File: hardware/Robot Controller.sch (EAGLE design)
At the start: 7 parts

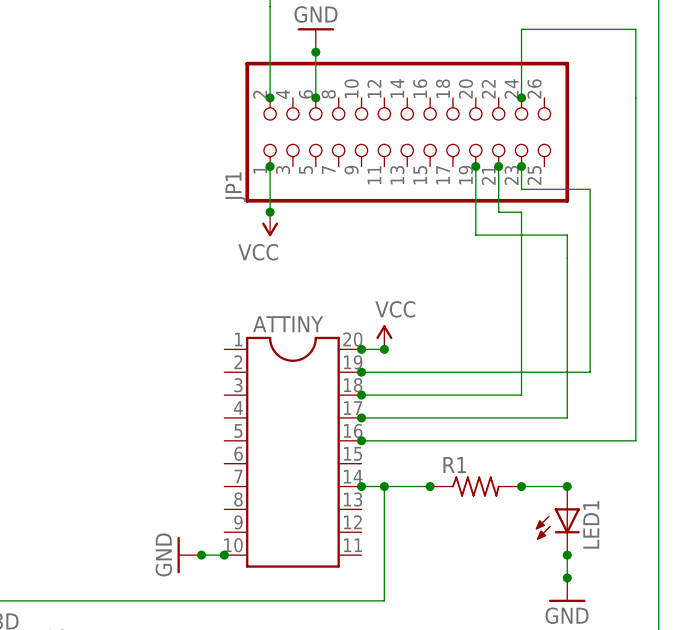
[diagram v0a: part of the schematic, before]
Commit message: added a host pin
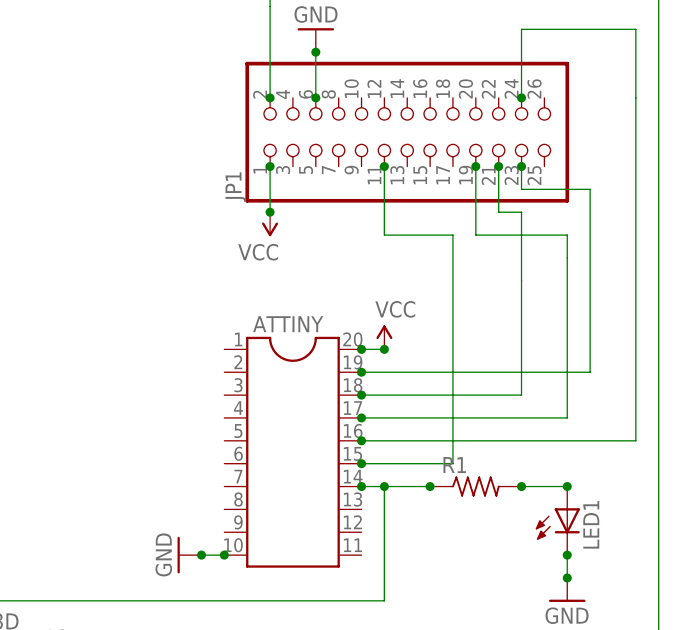
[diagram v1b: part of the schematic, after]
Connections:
- new net N$2: ATTINY.15, JP1.11
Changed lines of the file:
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@@
+</segment>
+</net>
+<net name="N$2" class="0">
+<segment>
+<pinref part="JP1" gate="A" pin="11"/>
+<wire x1="68.58" y1="93.98" x2="68.58" y2="86.36" width="0.1524" layer="91"/>
+<wire x1="68.58" y1="86.36" x2="76.2" y2="86.36" width="0.1524" layer="91"/>
+<wire x1="76.2" y1="86.36" x2="76.2" y2="60.96" width="0.1524" layer="91"/>
+<pinref part="ATTINY" gate="G$1" pin="15"/>
+<wire x1="76.2" y1="60.96" x2="66.04" y2="60.96" width="0.1524" layer="91"/>
+<junction x="66.04" y="60.96"/>
+<junction x="68.58" y="93.98"/>
 </segment>
 </net>

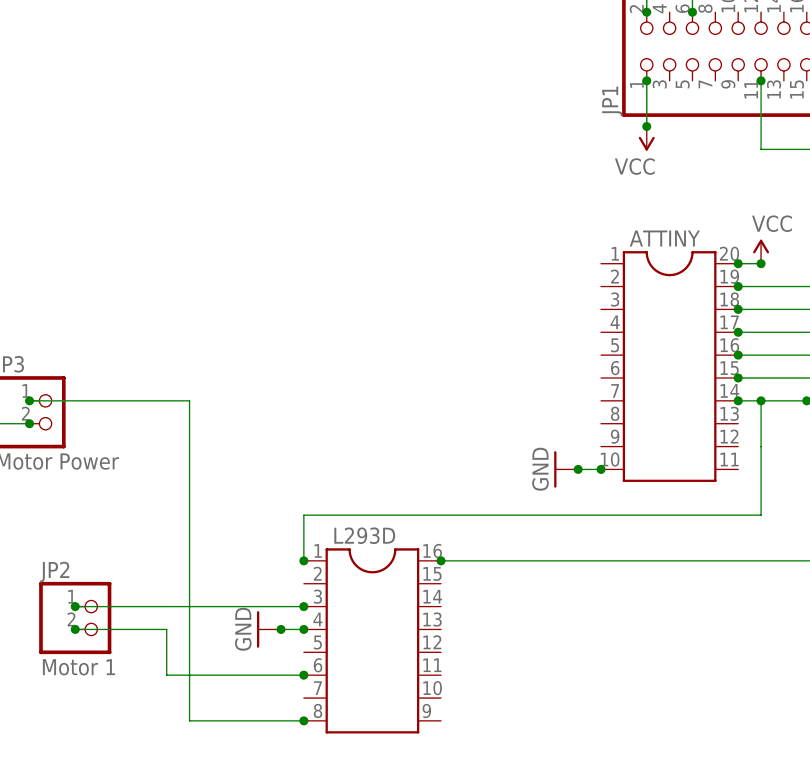
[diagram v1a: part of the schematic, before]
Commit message: thinking out how motor direction will be controlled
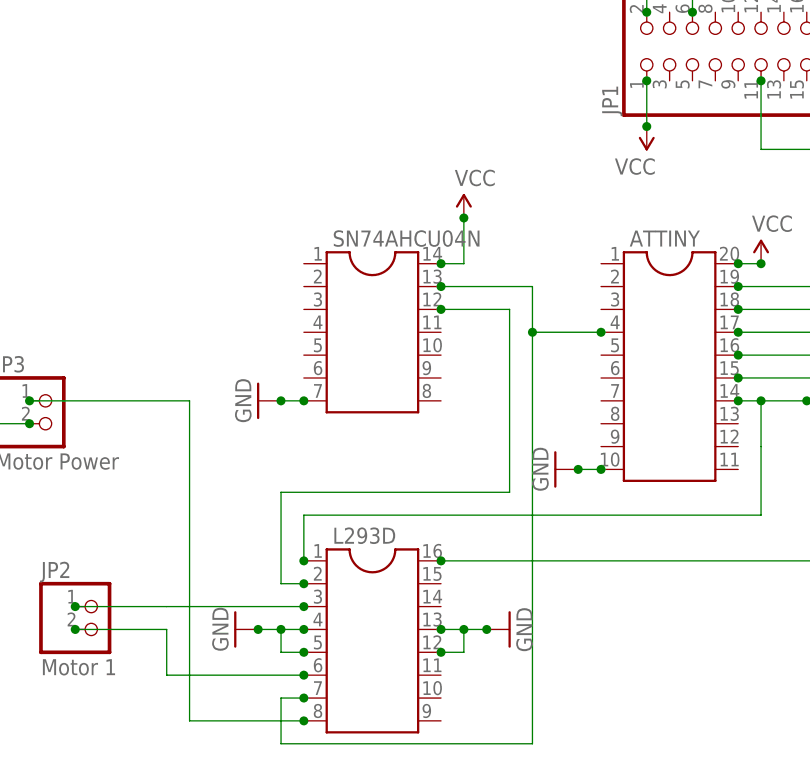
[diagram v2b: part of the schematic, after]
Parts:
- added SN74AHCU04N: (no value), ic-package:DIL14S
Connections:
- new net N$13: ATTINY.4, L293D.7, SN74AHCU04N.13
- new net N$15: L293D.2, SN74AHCU04N.12
- net GND: now also L293D.12, L293D.13, L293D.5, SN74AHCU04N.7
- net VCC: now also SN74AHCU04N.14
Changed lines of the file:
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@@
 <part name="SUPPLY1" library="SparkFun-Aesthetics" deviceset="VCC" device=""/>
 <part name="SUPPLY2" library="SparkFun-Aesthetics" deviceset="VCC" device=""/>
+<part name="GND6" library="SparkFun-Aesthetics" deviceset="GND" device=""/>
+<part name="SN74AHCU04N" library="ic-package" deviceset="DIL14" device="S"/>
+<part name="GND7" library="SparkFun-Aesthetics" deviceset="GND" device=""/>
+<part name="SUPPLY3" library="SparkFun-Aesthetics" deviceset="VCC" device=""/>
 </parts>
 <sheets>
@@
 <instance part="GND3" gate="1" x="-22.86" y="53.34"/>
 <instance part="GND4" gate="1" x="45.72" y="50.8" rot="R270"/>
-<instance part="GND5" gate="1" x="12.7" y="33.02" rot="R270"/>
+<instance part="GND5" gate="1" x="10.16" y="33.02" rot="R270"/>
 <instance part="SUPPLY1" gate="1" x="55.88" y="88.9" rot="R180"/>
 <instance part="SUPPLY2" gate="1" x="68.58" y="73.66"/>
+<instance part="GND6" gate="1" x="40.64" y="33.02" rot="R90"/>
+<instance part="SN74AHCU04N" gate="G$1" x="25.4" y="66.04"/>
+<instance part="GND7" gate="1" x="12.7" y="58.42" rot="R270"/>
+<instance part="SUPPLY3" gate="1" x="35.56" y="78.74"/>
 </instances>
 <busses>
@@
 <segment>
 <pinref part="GND5" gate="1" pin="GND"/>
-<wire x1="15.24" y1="33.02" x2="17.78" y2="33.02" width="0.1524" layer="91"/>
-<junction x="15.24" y="33.02"/>
+<wire x1="12.7" y1="33.02" x2="15.24" y2="33.02" width="0.1524" layer="91"/>
+<junction x="12.7" y="33.02"/>
 <pinref part="L293D" gate="G$1" pin="4"/>
 <junction x="17.78" y="33.02"/>
+<pinref part="L293D" gate="G$1" pin="5"/>
+<wire x1="15.24" y1="33.02" x2="17.78" y2="33.02" width="0.1524" layer="91"/>
+<wire x1="17.78" y1="30.48" x2="15.24" y2="30.48" width="0.1524" layer="91"/>
+<wire x1="15.24" y1="30.48" x2="15.24" y2="33.02" width="0.1524" layer="91"/>
+<junction x="17.78" y="30.48"/>
+<junction x="15.24" y="33.02"/>
 </segment>
 <segment>
@@
 <junction x="50.8" y="50.8"/>
 </segment>
+<segment>
+<pinref part="L293D" gate="G$1" pin="13"/>
+<pinref part="GND6" gate="1" pin="GND"/>
+<wire x1="33.02" y1="33.02" x2="35.56" y2="33.02" width="0.1524" layer="91"/>
+<pinref part="L293D" gate="G$1" pin="12"/>
+<wire x1="35.56" y1="33.02" x2="38.1" y2="33.02" width="0.1524" layer="91"/>
+<wire x1="33.02" y1="30.48" x2="35.56" y2="30.48" width="0.1524" layer="91"/>
+<wire x1="35.56" y1="30.48" x2="35.56" y2="33.02" width="0.1524" layer="91"/>
+<junction x="33.02" y="30.48"/>
+<junction x="35.56" y="33.02"/>
+<junction x="33.02" y="33.02"/>
+<junction x="38.1" y="33.02"/>
+</segment>
+<segment>
+<pinref part="SN74AHCU04N" gate="G$1" pin="7"/>
+<pinref part="GND7" gate="1" pin="GND"/>
+<wire x1="17.78" y1="58.42" x2="15.24" y2="58.42" width="0.1524" layer="91"/>
+<junction x="17.78" y="58.42"/>
+<junction x="15.24" y="58.42"/>
+</segment>
 </net>
 <net name="VCC" class="0">
@@
 <junction x="66.04" y="73.66"/>
 <junction x="68.58" y="73.66"/>
+</segment>
+<segment>
+<pinref part="SN74AHCU04N" gate="G$1" pin="14"/>
+<wire x1="33.02" y1="73.66" x2="35.56" y2="73.66" width="0.1524" layer="91"/>
+<pinref part="SUPPLY3" gate="1" pin="VCC"/>
+<wire x1="35.56" y1="73.66" x2="35.56" y2="78.74" width="0.1524" layer="91"/>
+<junction x="33.02" y="73.66"/>
+<junction x="35.56" y="78.74"/>
 </segment>
 </net>
@@
 </segment>
 </net>
+<net name="N$13" class="0">
+<segment>
+<pinref part="ATTINY" gate="G$1" pin="4"/>
+<wire x1="50.8" y1="66.04" x2="43.18" y2="66.04" width="0.1524" layer="91"/>
+<wire x1="43.18" y1="66.04" x2="43.18" y2="71.12" width="0.1524" layer="91"/>
+<pinref part="SN74AHCU04N" gate="G$1" pin="13"/>
+<wire x1="43.18" y1="71.12" x2="33.02" y2="71.12" width="0.1524" layer="91"/>
+<junction x="33.02" y="71.12"/>
+<junction x="50.8" y="66.04"/>
+<pinref part="L293D" gate="G$1" pin="7"/>
+<wire x1="17.78" y1="25.4" x2="15.24" y2="25.4" width="0.1524" layer="91"/>
+<wire x1="15.24" y1="25.4" x2="15.24" y2="20.32" width="0.1524" layer="91"/>
+<wire x1="15.24" y1="20.32" x2="43.18" y2="20.32" width="0.1524" layer="91"/>
+<wire x1="43.18" y1="20.32" x2="43.18" y2="66.04" width="0.1524" layer="91"/>
+<junction x="43.18" y="66.04"/>
+<junction x="17.78" y="25.4"/>
+</segment>
+</net>
+<net name="N$15" class="0">
+<segment>
+<pinref part="L293D" gate="G$1" pin="2"/>
+<wire x1="17.78" y1="38.1" x2="15.24" y2="38.1" width="0.1524" layer="91"/>
+<wire x1="15.24" y1="38.1" x2="15.24" y2="48.26" width="0.1524" layer="91"/>
+<wire x1="15.24" y1="48.26" x2="40.64" y2="48.26" width="0.1524" layer="91"/>
+<wire x1="40.64" y1="48.26" x2="40.64" y2="68.58" width="0.1524" layer="91"/>
+<pinref part="SN74AHCU04N" gate="G$1" pin="12"/>
+<wire x1="40.64" y1="68.58" x2="33.02" y2="68.58" width="0.1524" layer="91"/>
+<junction x="33.02" y="68.58"/>
+<junction x="17.78" y="38.1"/>
+</segment>
+</net>

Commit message: tweak hardware design
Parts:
- removed JP2: Motor 1, pinhead:PINHD-1X2
- removed JP3: Motor Power, pinhead:PINHD-1X2
- added H1, H2: MOUNT-HOLE2.8, holes:MOUNT-HOLE2.8
- added LED2: (no value), led:LEDSMT1206
- added R2: (no value), resistor:R-US_R3216
- added SL1, SL2: (no value), con-amp-quick:M02
- LED1: device led:LED5MM -> led:LEDSMT1206
- R1: device resistor:R-US_R6332 -> resistor:R-US_R3216
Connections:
- removed net N$11: LED1.A, R1.2
- new net N$16: ATTINY.2, R2.1
- new net N$17: LED2.A, R2.2
- new net N$3: LED1.A, R1.1
- net GND: now also LED2.C, SL2.2; no longer JP3.2
- net N$1: now also R1.2; no longer R1.1
- net N$10: now also SL2.1; no longer JP3.1
- net N$8: now also SL1.2; no longer JP2.1
- net N$9: now also SL1.1; no longer JP2.2
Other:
- moved on the sheet: R1
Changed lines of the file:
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@@
 <part name="ATTINY" library="ic-package" deviceset="DIL20" device="S"/>
 <part name="JP1" library="pinhead" deviceset="PINHD-2X13" device=""/>
-<part name="JP2" library="pinhead" deviceset="PINHD-1X2" device="" value="Motor 1"/>
-<part name="JP3" library="pinhead" deviceset="PINHD-1X2" device="" value="Motor Power"/>
-<part name="R1" library="resistor" deviceset="R-US_" device="R6332"/>
-<part name="LED1" library="led" deviceset="LED" device="5MM"/>
 <part name="GND1" library="SparkFun-Aesthetics" deviceset="GND" device=""/>
 <part name="GND2" library="SparkFun-Aesthetics" deviceset="GND" device=""/>
@@
 <part name="GND7" library="SparkFun-Aesthetics" deviceset="GND" device=""/>
 <part name="SUPPLY3" library="SparkFun-Aesthetics" deviceset="VCC" device=""/>
+<part name="R2" library="resistor" deviceset="R-US_" device="R3216"/>
+<part name="LED2" library="led" deviceset="LED" device="SMT1206"/>
+<part name="GND8" library="SparkFun-Aesthetics" deviceset="GND" device=""/>
+<part name="R1" library="resistor" deviceset="R-US_" device="R3216"/>
+<part name="LED1" library="led" deviceset="LED" device="SMT1206"/>
+<part name="SL1" library="con-amp-quick" deviceset="M02" device=""/>
+<part name="SL2" library="con-amp-quick" deviceset="M02" device=""/>
+<part name="H1" library="holes" deviceset="MOUNT-HOLE" device="2.8"/>
+<part name="H2" library="holes" deviceset="MOUNT-HOLE" device="2.8"/>
 </parts>
 <sheets>
@@
 <instance part="ATTINY" gate="G$1" x="58.42" y="63.5"/>
 <instance part="JP1" gate="A" x="71.12" y="96.52" rot="R90"/>
-<instance part="JP2" gate="G$1" x="-5.08" y="33.02"/>
-<instance part="JP3" gate="G$1" x="-10.16" y="55.88"/>
-<instance part="R1" gate="G$1" x="78.74" y="58.42"/>
-<instance part="LED1" gate="G$1" x="88.9" y="55.88"/>
 <instance part="GND1" gate="1" x="60.96" y="109.22" rot="R180"/>
 <instance part="GND2" gate="1" x="88.9" y="45.72"/>
 <instance part="GND3" gate="1" x="-22.86" y="53.34"/>
 <instance part="GND4" gate="1" x="45.72" y="50.8" rot="R270"/>
-<instance part="GND5" gate="1" x="10.16" y="33.02" rot="R270"/>
+<instance part="GND5" gate="1" x="12.7" y="33.02" rot="R270"/>
 <instance part="SUPPLY1" gate="1" x="55.88" y="88.9" rot="R180"/>
 <instance part="SUPPLY2" gate="1" x="68.58" y="73.66"/>
-<instance part="GND6" gate="1" x="40.64" y="33.02" rot="R90"/>
+<instance part="GND6" gate="1" x="38.1" y="33.02" rot="R90"/>
 <instance part="SN74AHCU04N" gate="G$1" x="25.4" y="66.04"/>
 <instance part="GND7" gate="1" x="12.7" y="58.42" rot="R270"/>
 <instance part="SUPPLY3" gate="1" x="35.56" y="78.74"/>
+<instance part="R2" gate="G$1" x="43.18" y="93.98" rot="R90"/>
+<instance part="LED2" gate="G$1" x="43.18" y="104.14" rot="R180"/>
+<instance part="GND8" gate="1" x="43.18" y="114.3" rot="R180"/>
+<instance part="R1" gate="G$1" x="78.74" y="58.42" rot="R180"/>
+<instance part="LED1" gate="G$1" x="88.9" y="55.88"/>
+<instance part="SL1" gate="G$1" x="-10.16" y="33.02"/>
+<instance part="SL2" gate="G$1" x="-10.16" y="48.26" rot="R90"/>
+<instance part="H1" gate="G$1" x="-35.56" y="114.3"/>
+<instance part="H2" gate="G$1" x="-35.56" y="106.68"/>
 </instances>
 <busses>
@@
 <junction x="66.04" y="58.42"/>
 <wire x1="68.58" y1="58.42" x2="73.66" y2="58.42" width="0.1524" layer="91"/>
-<pinref part="R1" gate="G$1" pin="1"/>
 <junction x="68.58" y="58.42"/>
+<pinref part="R1" gate="G$1" pin="2"/>
 <junction x="73.66" y="58.42"/>
 </segment>
@@
 <net name="N$8" class="0">
 <segment>
-<wire x1="-7.62" y1="35.56" x2="2.54" y2="35.56" width="0.1524" layer="91"/>
 <pinref part="L293D" gate="G$1" pin="3"/>
 <wire x1="2.54" y1="35.56" x2="17.78" y2="35.56" width="0.1524" layer="91"/>
 <junction x="17.78" y="35.56"/>
-<pinref part="JP2" gate="G$1" pin="1"/>
-<junction x="-7.62" y="35.56"/>
+<pinref part="SL1" gate="G$1" pin="2"/>
+<wire x1="2.54" y1="35.56" x2="-2.54" y2="35.56" width="0.1524" layer="91"/>
+<junction x="-2.54" y="35.56"/>
 </segment>
 </net>
@@
 <junction x="17.78" y="27.94"/>
 <wire x1="2.54" y1="27.94" x2="2.54" y2="33.02" width="0.1524" layer="91"/>
-<pinref part="JP2" gate="G$1" pin="2"/>
-<wire x1="2.54" y1="33.02" x2="-7.62" y2="33.02" width="0.1524" layer="91"/>
-<junction x="-7.62" y="33.02"/>
+<pinref part="SL1" gate="G$1" pin="1"/>
+<wire x1="2.54" y1="33.02" x2="-2.54" y2="33.02" width="0.1524" layer="91"/>
+<junction x="-2.54" y="33.02"/>
 </segment>
 </net>
 <net name="N$10" class="0">
 <segment>
-<pinref part="JP3" gate="G$1" pin="1"/>
-<wire x1="-12.7" y1="58.42" x2="5.08" y2="58.42" width="0.1524" layer="91"/>
-<wire x1="5.08" y1="58.42" x2="5.08" y2="22.86" width="0.1524" layer="91"/>
+<wire x1="-10.16" y1="55.88" x2="5.08" y2="55.88" width="0.1524" layer="91"/>
+<wire x1="5.08" y1="55.88" x2="5.08" y2="22.86" width="0.1524" layer="91"/>
 <pinref part="L293D" gate="G$1" pin="8"/>
 <wire x1="5.08" y1="22.86" x2="17.78" y2="22.86" width="0.1524" layer="91"/>
-<junction x="-12.7" y="58.42"/>
 <junction x="17.78" y="22.86"/>
+<pinref part="SL2" gate="G$1" pin="1"/>
+<junction x="-10.16" y="55.88"/>
 </segment>
 </net>
@@
 </segment>
 </net>
-<net name="N$11" class="0">
-<segment>
-<pinref part="R1" gate="G$1" pin="2"/>
-<pinref part="LED1" gate="G$1" pin="A"/>
-<wire x1="83.82" y1="58.42" x2="88.9" y2="58.42" width="0.1524" layer="91"/>
-<junction x="88.9" y="58.42"/>
-<junction x="83.82" y="58.42"/>
-</segment>
-</net>
 <net name="GND" class="0">
 <segment>
@@
 </segment>
 <segment>
-<pinref part="LED1" gate="G$1" pin="C"/>
 <pinref part="GND2" gate="1" pin="GND"/>
 <wire x1="88.9" y1="50.8" x2="88.9" y2="48.26" width="0.1524" layer="91"/>
+<junction x="88.9" y="48.26"/>
+<pinref part="LED1" gate="G$1" pin="C"/>
 <junction x="88.9" y="50.8"/>
-<junction x="88.9" y="48.26"/>
 </segment>
 <segment>
 <pinref part="GND3" gate="1" pin="GND"/>
-<pinref part="JP3" gate="G$1" pin="2"/>
 <wire x1="-22.86" y1="55.88" x2="-12.7" y2="55.88" width="0.1524" layer="91"/>
 <junction x="-22.86" y="55.88"/>
+<pinref part="SL2" gate="G$1" pin="2"/>
 <junction x="-12.7" y="55.88"/>
 </segment>
 <segment>
 <pinref part="GND5" gate="1" pin="GND"/>
-<wire x1="12.7" y1="33.02" x2="15.24" y2="33.02" width="0.1524" layer="91"/>
-<junction x="12.7" y="33.02"/>
+<junction x="15.24" y="33.02"/>
 <pinref part="L293D" gate="G$1" pin="4"/>
 <junction x="17.78" y="33.02"/>
@@
 <wire x1="33.02" y1="33.02" x2="35.56" y2="33.02" width="0.1524" layer="91"/>
 <pinref part="L293D" gate="G$1" pin="12"/>
-<wire x1="35.56" y1="33.02" x2="38.1" y2="33.02" width="0.1524" layer="91"/>
 <wire x1="33.02" y1="30.48" x2="35.56" y2="30.48" width="0.1524" layer="91"/>
 <wire x1="35.56" y1="30.48" x2="35.56" y2="33.02" width="0.1524" layer="91"/>
@@
 <junction x="35.56" y="33.02"/>
 <junction x="33.02" y="33.02"/>
-<junction x="38.1" y="33.02"/>
+<junction x="35.56" y="33.02"/>
 </segment>
 <segment>
@@
 <junction x="17.78" y="58.42"/>
 <junction x="15.24" y="58.42"/>
+</segment>
+<segment>
+<pinref part="LED2" gate="G$1" pin="C"/>
+<pinref part="GND8" gate="1" pin="GND"/>
+<wire x1="43.18" y1="109.22" x2="43.18" y2="111.76" width="0.1524" layer="91"/>
+<junction x="43.18" y="109.22"/>
+<junction x="43.18" y="111.76"/>
 </segment>
 </net>
@@
 <segment>
 <pinref part="JP1" gate="A" pin="11"/>
-<wire x1="68.58" y1="93.98" x2="68.58" y2="86.36" width="0.1524" layer="91"/>
-<wire x1="68.58" y1="86.36" x2="76.2" y2="86.36" width="0.1524" layer="91"/>
-<wire x1="76.2" y1="86.36" x2="76.2" y2="60.96" width="0.1524" layer="91"/>
+<wire x1="68.58" y1="93.98" x2="68.58" y2="86.36" width="0.1524" layer="91" style="shortdash"/>
+<wire x1="68.58" y1="86.36" x2="76.2" y2="86.36" width="0.1524" layer="91" style="shortdash"/>
+<wire x1="76.2" y1="86.36" x2="76.2" y2="60.96" width="0.1524" layer="91" style="shortdash"/>
 <pinref part="ATTINY" gate="G$1" pin="15"/>
-<wire x1="76.2" y1="60.96" x2="66.04" y2="60.96" width="0.1524" layer="91"/>
+<wire x1="76.2" y1="60.96" x2="66.04" y2="60.96" width="0.1524" layer="91" style="shortdash"/>
 <junction x="66.04" y="60.96"/>
 <junction x="68.58" y="93.98"/>
@@
 </segment>
 </net>
+<net name="N$16" class="0">
+<segment>
+<pinref part="R2" gate="G$1" pin="1"/>
+<wire x1="43.18" y1="88.9" x2="43.18" y2="73.66" width="0.1524" layer="91"/>
+<wire x1="43.18" y1="73.66" x2="45.72" y2="73.66" width="0.1524" layer="91"/>
+<wire x1="45.72" y1="73.66" x2="45.72" y2="71.12" width="0.1524" layer="91"/>
+<pinref part="ATTINY" gate="G$1" pin="2"/>
+<wire x1="45.72" y1="71.12" x2="50.8" y2="71.12" width="0.1524" layer="91"/>
+<junction x="50.8" y="71.12"/>
+<junction x="43.18" y="88.9"/>
+</segment>
+</net>
+<net name="N$17" class="0">
+<segment>
+<pinref part="R2" gate="G$1" pin="2"/>
+<pinref part="LED2" gate="G$1" pin="A"/>
+<wire x1="43.18" y1="99.06" x2="43.18" y2="101.6" width="0.1524" layer="91"/>
+<junction x="43.18" y="99.06"/>
+<junction x="43.18" y="101.6"/>
+</segment>
+</net>
+<net name="N$3" class="0">
+<segment>
+<pinref part="R1" gate="G$1" pin="1"/>
+<pinref part="LED1" gate="G$1" pin="A"/>
+<wire x1="83.82" y1="58.42" x2="88.9" y2="58.42" width="0.1524" layer="91"/>
+<junction x="83.82" y="58.42"/>
+<junction x="88.9" y="58.42"/>
+</segment>
+</net>

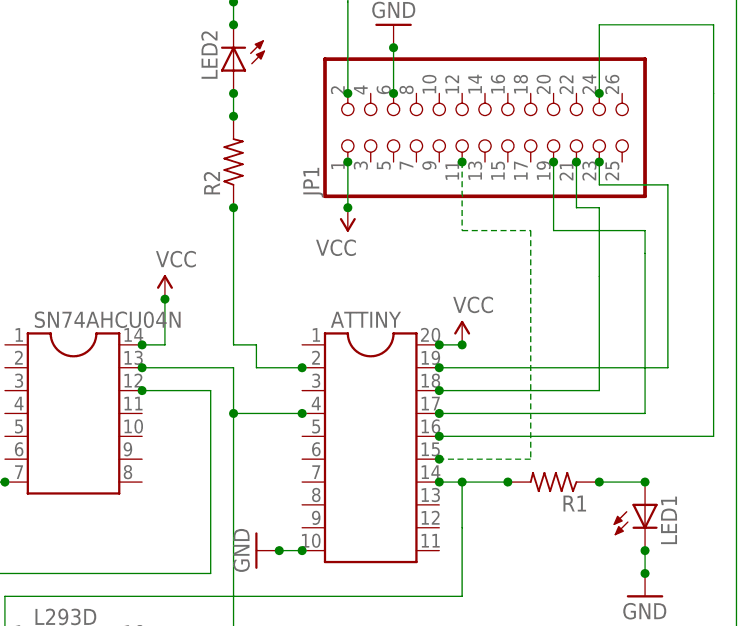
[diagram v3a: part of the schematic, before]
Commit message: change host pin
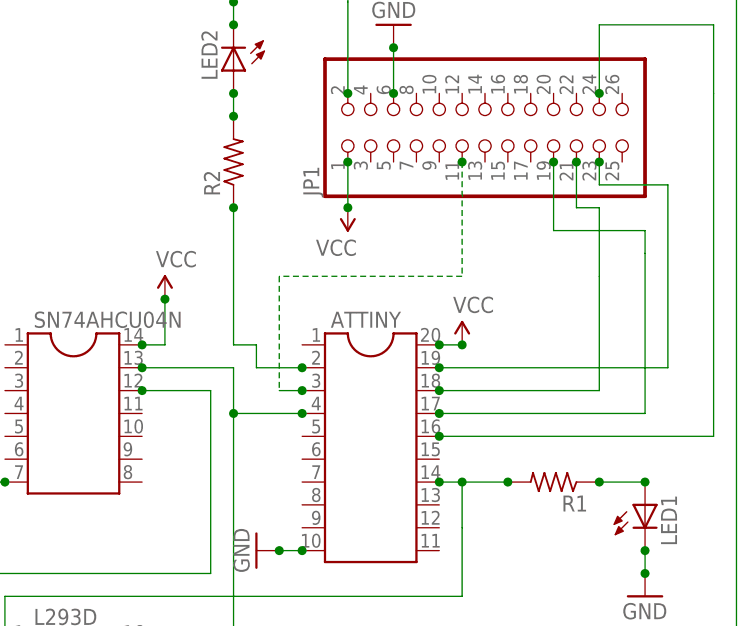
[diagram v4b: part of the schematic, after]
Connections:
- net N$2: now also ATTINY.3; no longer ATTINY.15
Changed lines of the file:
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@@
 <segment>
 <pinref part="JP1" gate="A" pin="11"/>
-<wire x1="68.58" y1="93.98" x2="68.58" y2="86.36" width="0.1524" layer="91" style="shortdash"/>
-<wire x1="68.58" y1="86.36" x2="76.2" y2="86.36" width="0.1524" layer="91" style="shortdash"/>
-<wire x1="76.2" y1="86.36" x2="76.2" y2="60.96" width="0.1524" layer="91" style="shortdash"/>
-<pinref part="ATTINY" gate="G$1" pin="15"/>
-<wire x1="76.2" y1="60.96" x2="66.04" y2="60.96" width="0.1524" layer="91" style="shortdash"/>
-<junction x="66.04" y="60.96"/>
+<wire x1="68.58" y1="93.98" x2="68.58" y2="81.28" width="0.1524" layer="91" style="shortdash"/>
+<wire x1="68.58" y1="81.28" x2="48.26" y2="81.28" width="0.1524" layer="91" style="shortdash"/>
+<wire x1="48.26" y1="81.28" x2="48.26" y2="68.58" width="0.1524" layer="91" style="shortdash"/>
 <junction x="68.58" y="93.98"/>
+<pinref part="ATTINY" gate="G$1" pin="3"/>
+<wire x1="48.26" y1="68.58" x2="50.8" y2="68.58" width="0.1524" layer="91"/>
+<junction x="50.8" y="68.58"/>
 </segment>
 </net>
